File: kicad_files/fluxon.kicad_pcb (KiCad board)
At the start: 2 copper layers, 241.6 x 72.1 mm, 159 parts, among them J1 Conn_ARM_JTAG_SWD_10, J2 U-F-M5DD-W-2, Q1 DTC123JKAT146, Q2 AO3402, SW1 ESC, SW10 O, SW11 P, SW12 DEL, SW13 BKSP, SW14 TAB_125, SW15 A, SW16 S, SW17 D, SW18 F, SW19 G, SW2 Q, SW20 H, SW21 J, SW22 K, SW23 L, SW24 QUOTE, SW25 ENTER_175, SW26 LSHIFT_175, SW27 Z, SW28 X, SW29 C, SW3 W, SW30 V, SW31 B, SW32 N, SW33 M, SW34 COMMA, SW35 DOT, SW36 RSHIFT_125, SW37 FN_100, SW38 RSHIFT_225, SW39 LCTRL_125, SW4 E, SW40 SUPER_100, SW41 LALT_100, SW42 SPC_625, SW43 RALT_125, SW44 RGUI_100, SW45 RCTRL_125, SW46 PN_100, SW47 SPC_175, SW48 SPC_275, SW49 FN_100, SW5 R, SW50 RALT_100, SW51 LCTRL_150, SW52 LALT_150, SW53 SPC_700, SW54 RCTRL_150, SW55 RALT_150, SW56 SW_Push, SW57 Rotary_Encoder_Switch_Chassis, SW6 T, SW7 Y, SW8 U, SW9 I, U1 USBLC6-2SC6, U2 STM32F072CBT6, U3 MCP1700-3302E/TT

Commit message: Add software reset circuit
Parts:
- removed the C10 at (-4.45, 46.4)
- removed the C11 at (20.3, 67.1)
- removed the C12 at (20.4, 78.9)
- removed R13: 1M, acheron_Components:R_SMD_1206
- removed R15, R16, R17, R18: 10k, acheron_Components:R_SMD_1206
- added Q3: DTA143EKAT146, Package_TO_SOT_SMD:SOT-23, F.Cu at (114.6, 104.8)
- added R1: 100, acheron_Components:R_SMD_1206, F.Cu at (114.1, 109.3)
- added SW58: BKSP_2U, acheron_MX_SolderMask:MX200, F.Cu at (31.3, 55.9)
- added SW59: (I) SLASH_100, acheron_MX_SolderMask:MX100, F.Cu at (45.6, 94.0)
- C10: renamed from CB2; value 100nF -> 100n
- C12: renamed from CB4; value 4.7uF -> 4.7u
- C13: renamed from CB5; value 1uF -> 1u
- C16: renamed from CB8; value 4.7uF -> 4.7u
- SW36: value RSHIFT_125 -> (D) RSHIFT_125
- SW37: value FN_100 -> (D) FN_100
- SW38: value RSHIFT_225 -> (F) RSHIFT_225
- SW57: value Rotary_Encoder_Switch_Chassis -> (I) RSHIFT_125; footprint acheron_Hardware:ALPS_EC11E -> acheron_MX_SolderMask:MX125
- moved SW57 38.2 mm to (24.1, 94.0)
- moved D13 9.53 mm to (26.5, 60.7)
- moved D36 4.91 mm to (40.8, 103.6)
- moved D37 3.85 mm to (28.6, 102.5), turned to 180 degrees
- renumbered CB1 to C1, CB3 to C11, CB6 to C14, CB7 to C15
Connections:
- D13 pad 2: M1 -> Net-(D13-Pad2)
- SW13 pad 1: M1 -> Net-(D13-Pad2)
- U2 pad 40: Col12 -> Net-(U2-Pad40)
- U2 pad 41: ROT_B -> SOFT_RESET
- U2 pad 42: ROT_A -> Col12
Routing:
- net ROT_A: track 247.9 -> 0.00 mm
- net ROT_B: track 243.2 -> 0.00 mm
- net SOFT_RESET: track 0.00 -> 136.8 mm, vias 0 -> 2
- net Net-(D13-Pad2): track 0.00 -> 24.6 mm
- net ENC_B: track 16.7 -> 0.00 mm
- net 3.3V: track 29.8 -> 43.4 mm
- net M1: track 11.0 -> 0.00 mm
- net Net-(D37-Pad2): track 6.54 -> 17.3 mm
- net ENC_A: track 8.35 -> 0.00 mm
- net Net-(D36-Pad2): track 18.1 -> 25.0 mm
- net Net-(D14-Pad2): track 0.00 -> 6.54 mm
- net BOOT0: track 8.54 -> 14.3 mm
- net Col12: track 294.1 -> 289.0 mm
- net Row4: track 297.0 -> 301.0 mm
- net Net-(Q3-Pad3): track 0.00 -> 3.58 mm
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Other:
- board text added: "(D) 1.25 RSFT"
- board text added: "(F) 2.25 RSFT"
- board text added: "(I) 1.00 SLSH"
- board text added: "(I) 1.25 RSFT"

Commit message: Finish routing
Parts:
- removed the Q1 at (108.6, 110.3)
- removed Q3: DTA143EKAT146, Package_TO_SOT_SMD:SOT-23
- added GR6: Warning Sign, acheron_Graphics:warning_sign_3.6x3.2mm, F.Cu at (36.6, 59.5)
- added J3: Conn_02x10, acheron_Connectors:PinHeader_2x8_P2.54mm_Vertical, F.Cu at (266.6, 102.8)
- added Q2: MUN5335DW1T1G, acheron_Components:SOT-363_SC-70-6, F.Cu at (122.2, 119.9)
- R8: renamed from R5; value 100K -> 100k
- R9: renamed from R6; value 100K -> 100k
- moved C16 354.4 mm to (247.8, 100.0), turned to 90 degrees
- moved C13 340.2 mm to (236.3, 95.9), turned to -90 degrees
- moved C15 316.1 mm to (248.9, 100.0), turned to 90 degrees
- moved C14 303.5 mm to (237.5, 95.9), turned to -90 degrees
- moved C12 297.1 mm to (248.9, 89.5), turned to 180 degrees
- moved C11 288.0 mm to (248.9, 90.6), turned to 180 degrees
- moved C9 275.8 mm to (238.5, 90.0)
- moved C10 274.9 mm to (237.7, 91.5), turned to 90 degrees
- moved C6 16.5 mm to (232.1, 75.3)
- moved D52 16.5 mm to (249.2, 71.1)
- moved Q1 16.5 mm to (262.6, 76.0)
- moved SW1 16.5 mm to (264.0, 65.1)
- moved C8 16.5 mm to (127.0, 126.1)
- moved D33 16.5 mm to (104.5, 108.0)
- moved R13 16.5 mm to (124.7, 124.0)
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- renumbered C9 to C1, C7 to C2, C8 to C3, C3 to C4, C2 to C7, C4 to C8, C1 to C9, D14 to D13, D15 to D14, D16 to D15, D17 to D16, D18 to D17, D19 to D18, D20 to D19, D21 to D20, D22 to D21, D23 to D22, D24 to D23, D25 to D24, D26 to D25, D27 to D26, D28 to D27, D29 to D28, D30 to D29, D31 to D30, D32 to D31, D33 to D32, D34 to D33, D35 to D34, D36 to D35, D37 to D36, D38 to D37, D39 to D38, D40 to D39, D41 to D40, D42 to D41, D43 to D42, D44 to D43, D13 to D44, D52 to D48, D53 to D49, D54 to D50, D50 to D51, D51 to D52, D49 to D53, Q2 to Q1, R9 to R1, R14 to R10, R1 to R11, R3 to R12, R4 to R13, R7 to R2, R8 to R3, R10 to R4, R11 to R5, R12 to R6, R2 to R7, SW14 to SW13, SW15 to SW14, SW16 to SW15, SW17 to SW16, SW18 to SW17, SW19 to SW18, SW20 to SW19, SW21 to SW20, SW22 to SW21, SW23 to SW22, SW24 to SW23, SW25 to SW24, SW26 to SW25, SW27 to SW26, SW28 to SW27, SW29 to SW28, SW30 to SW29, SW31 to SW30, SW32 to SW31, SW33 to SW32, SW34 to SW33, SW35 to SW34, SW36 to SW35, SW37 to SW36, SW38 to SW37, SW57 to SW38, SW59 to SW39, SW39 to SW40, SW40 to SW41, SW41 to SW42, SW42 to SW43, SW43 to SW44, SW44 to SW45, SW45 to SW46, SW13 to SW47, SW58 to SW48, SW46 to SW49, SW47 to SW50, SW48 to SW51, SW49 to SW52, SW50 to SW53, SW51 to SW54, SW52 to SW55, SW53 to SW56, SW54 to SW57, SW55 to SW58, SW56 to SW59, U3 to U2, U2 to U3
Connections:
- U3 pad 13: Net-(U2-Pad13) -> EXTRA18
- U3 pad 14: Net-(U2-Pad14) -> EXTRA17
- U3 pad 15: Net-(U2-Pad15) -> EXTRA16
- U3 pad 16: Net-(U2-Pad16) -> EXTRA15
- U3 pad 17: Net-(U2-Pad17) -> EXTRA14
- U3 pad 18: Net-(U2-Pad18) -> EXTRA13
- U3 pad 19: Net-(U2-Pad19) -> EXTRA12
- U3 pad 20: Net-(U2-Pad20) -> EXTRA11
- U3 pad 21: Net-(U2-Pad21) -> EXTRA10
- U3 pad 22: Net-(U2-Pad22) -> EXTRA9
- U3 pad 25: Net-(U2-Pad25) -> Col1
- U3 pad 27: Net-(U2-Pad27) -> EXTRA8
- U3 pad 29: Net-(U2-Pad29) -> EXTRA5
- U3 pad 30: Net-(U2-Pad30) -> EXTRA3
- U3 pad 31: Net-(U2-Pad31) -> EXTRA6
- U3 pad 38: Net-(U2-Pad38) -> Row1
- U3 pad 39: Net-(U2-Pad39) -> Row2
- U3 pad 40: Net-(U2-Pad40) -> SOFT_RESET
- U3 pad 41: SOFT_RESET -> Col12
- U3 pad 42: Col12 -> Row4
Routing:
- net 3.3V: track 43.4 -> 290.9 mm, vias 0 -> 6
- net Row4: track 301.0 -> 528.1 mm
- net SWDIO: track 0.00 -> 192.7 mm, vias 0 -> 1
- net SWCLK: track 0.00 -> 187.6 mm, vias 0 -> 1
- net BOOT0: track 14.3 -> 193.7 mm, vias 0 -> 2
- net NRST: track 11.6 -> 188.7 mm, vias 0 -> 2
- net Row1: track 191.1 -> 356.0 mm, vias 0 -> 2
- net Row3: track 213.5 -> 302.9 mm, vias 0 -> 2
- net EXTRA10: track 0.00 -> 40.5 mm
- net EXTRA12: track 0.00 -> 39.5 mm
- net EXTRA14: track 0.00 -> 39.4 mm
- net EXTRA16: track 0.00 -> 38.8 mm
- net EXTRA18: track 0.00 -> 37.5 mm
- net EXTRA9: track 0.00 -> 37.2 mm
- net EXTRA11: track 0.00 -> 36.2 mm
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- added copper zone on B.Cu, net 3.3V

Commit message: Quality of circuit improvements
- Adoption of STM32L072 MCU variant
- Changed TVS to SMF6.0A unidirectional
- Addition of regulation capacitor to voltage divider resistors in the level shifter circuit
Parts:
- added C17: 1u, Capacitor_SMD:C_0805_2012Metric_Pad1.15x1.40mm_HandSolder, F.Cu at (257.3, 73.8)
- D52: value SMF9.0CA -> SMF6.0A; footprint acheron_Components:D_SOD-123_Bidirectional -> acheron_Components:D_SOD-123
- Q1: value AO3402 -> BSS138
- R4, R6: value 10k -> 1k
- R5: value 5.1k -> 510R
- U3: value STM32F072CBT6 -> STM32L072CBT6
- moved D24 4.60 mm to (55.5, 79.4)
- moved GR6 0.37 mm to (36.5, 59.9)
- renumbered SW59 to S1
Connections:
- C2 pad 2: Net-(C7-Pad2) -> Net-(C2-Pad2)
- C5 pad 1: GND -> 5V
- C5 pad 2: 5V -> GND
- D49 pad 1: Net-(C7-Pad2) -> Net-(C2-Pad2)
- R2 pad 1: Net-(C7-Pad2) -> 5V
- R2 pad 2: 5V -> Net-(C2-Pad2)
- R5 pad 2: RGB_5V -> 5V
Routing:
- net 5V: track 253.4 -> 267.3 mm
- net Row2: track 225.9 -> 220.4 mm
- net Net-(C7-Pad2): track 4.79 -> 0.00 mm
- net Net-(D24-Pad2): track 4.76 -> 9.37 mm
- net Net-(C17-Pad2): track 4.69 -> 7.45 mm
- net RGB_5V: track 32.0 -> 29.4 mm
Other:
- board size 241.6 x 72.1 mm -> 241.6 x 71.7 mm
- net class Default removed

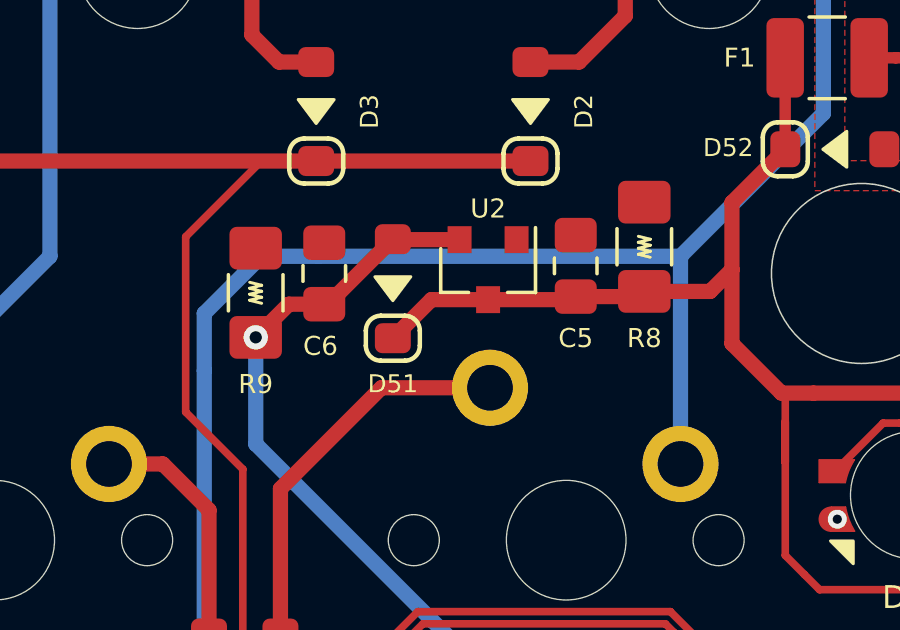
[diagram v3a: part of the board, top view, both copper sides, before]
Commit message: Change LDO bypass capacitors to tantallum
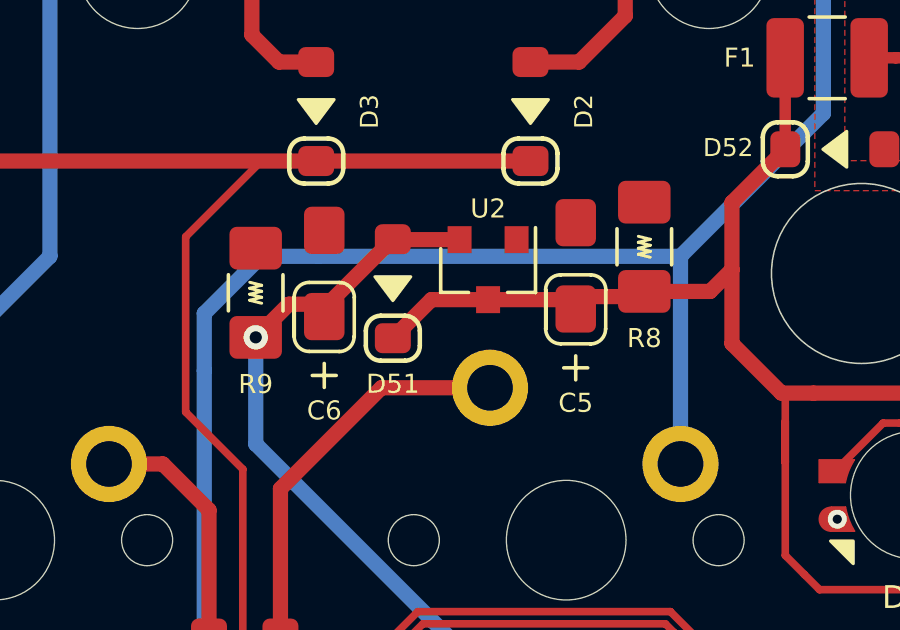
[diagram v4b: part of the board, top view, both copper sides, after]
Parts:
- C5: value 10u -> 1u; footprint Capacitor_SMD:C_0805_2012Metric_Pad1.15x1.40mm_HandSolder -> acheron_Components:CP_EIA-3216-10_Kemet-I_Pad1.58x1.35mm_HandSolder
- C6: footprint Capacitor_SMD:C_0805_2012Metric_Pad1.15x1.40mm_HandSolder -> acheron_Components:CP_EIA-3216-10_Kemet-I_Pad1.58x1.35mm_HandSolder
- turned C5 to 90 degrees
- turned C6 to 90 degrees
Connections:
- C6 pad 1: GND -> 3.3V
- C6 pad 2: 3.3V -> GND

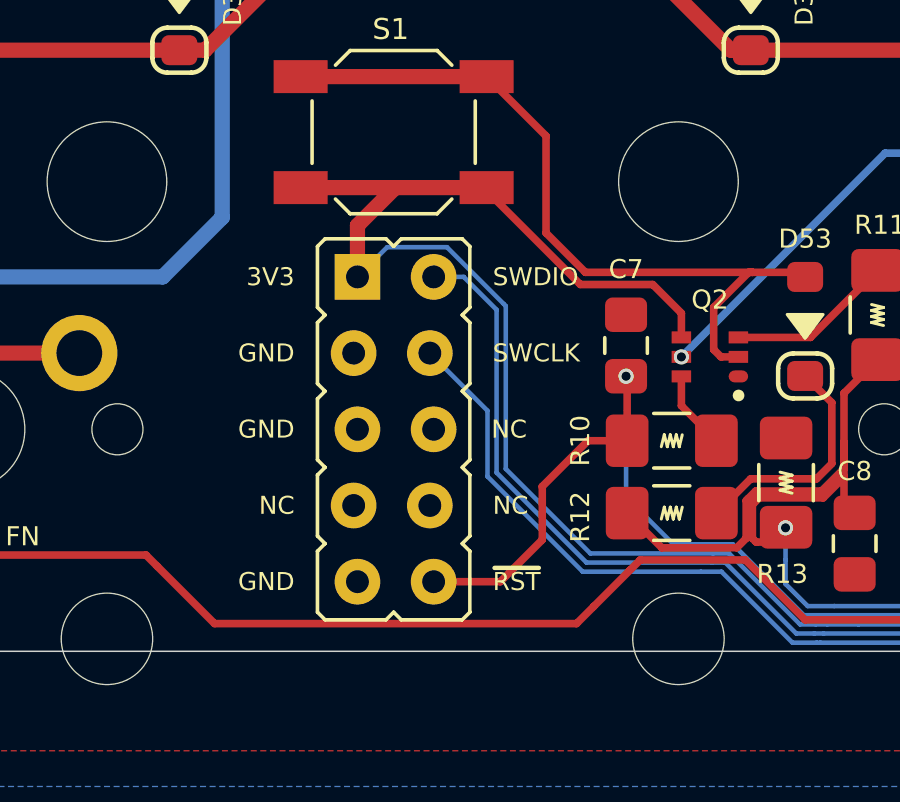
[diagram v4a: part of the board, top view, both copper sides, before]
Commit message: Change ARM SWD JTAG to 6 pin variant
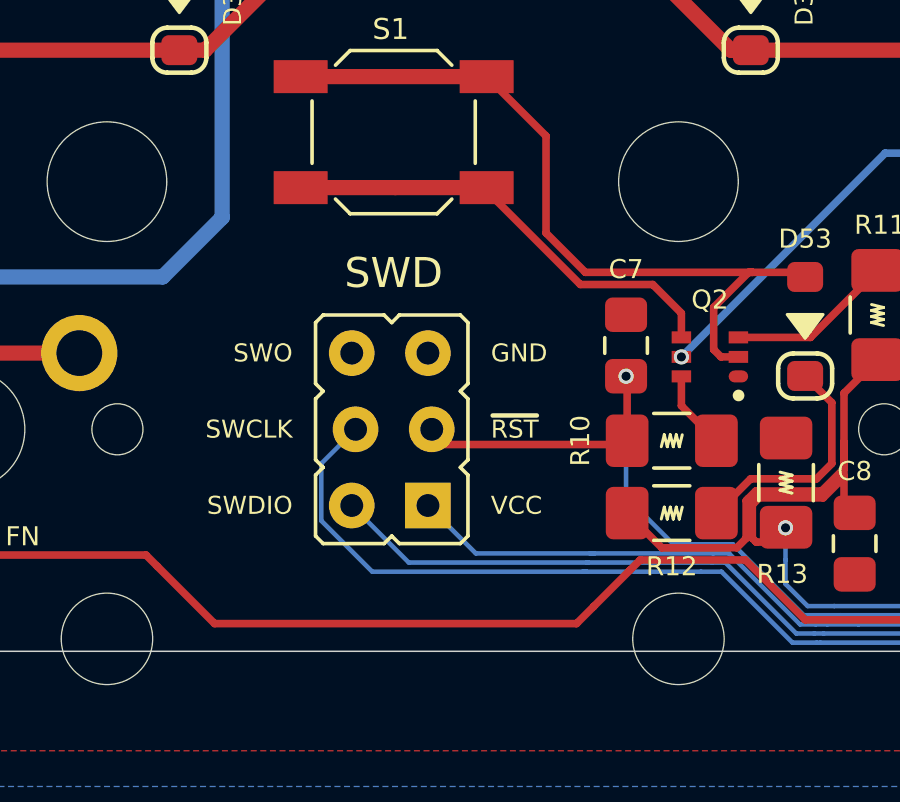
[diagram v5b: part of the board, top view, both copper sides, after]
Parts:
- J1: value Conn_ARM_JTAG_SWD_10 -> ARM SWD; footprint acheron_Connectors:Conn_ARM_JTAG_SWD_10 -> acheron_Connectors:Conn_ARM_JTAG_SWD_6
- turned J1 to 180 degrees
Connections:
- J1 pad 3: GND -> NRST
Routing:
- net 3.3V: track 290.9 -> 278.0 mm
- net SWCLK: track 187.6 -> 191.3 mm
- net SWDIO: track 192.7 -> 189.2 mm
- net NRST: track 188.7 -> 185.7 mm
